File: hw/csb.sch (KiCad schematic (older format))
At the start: 31 parts

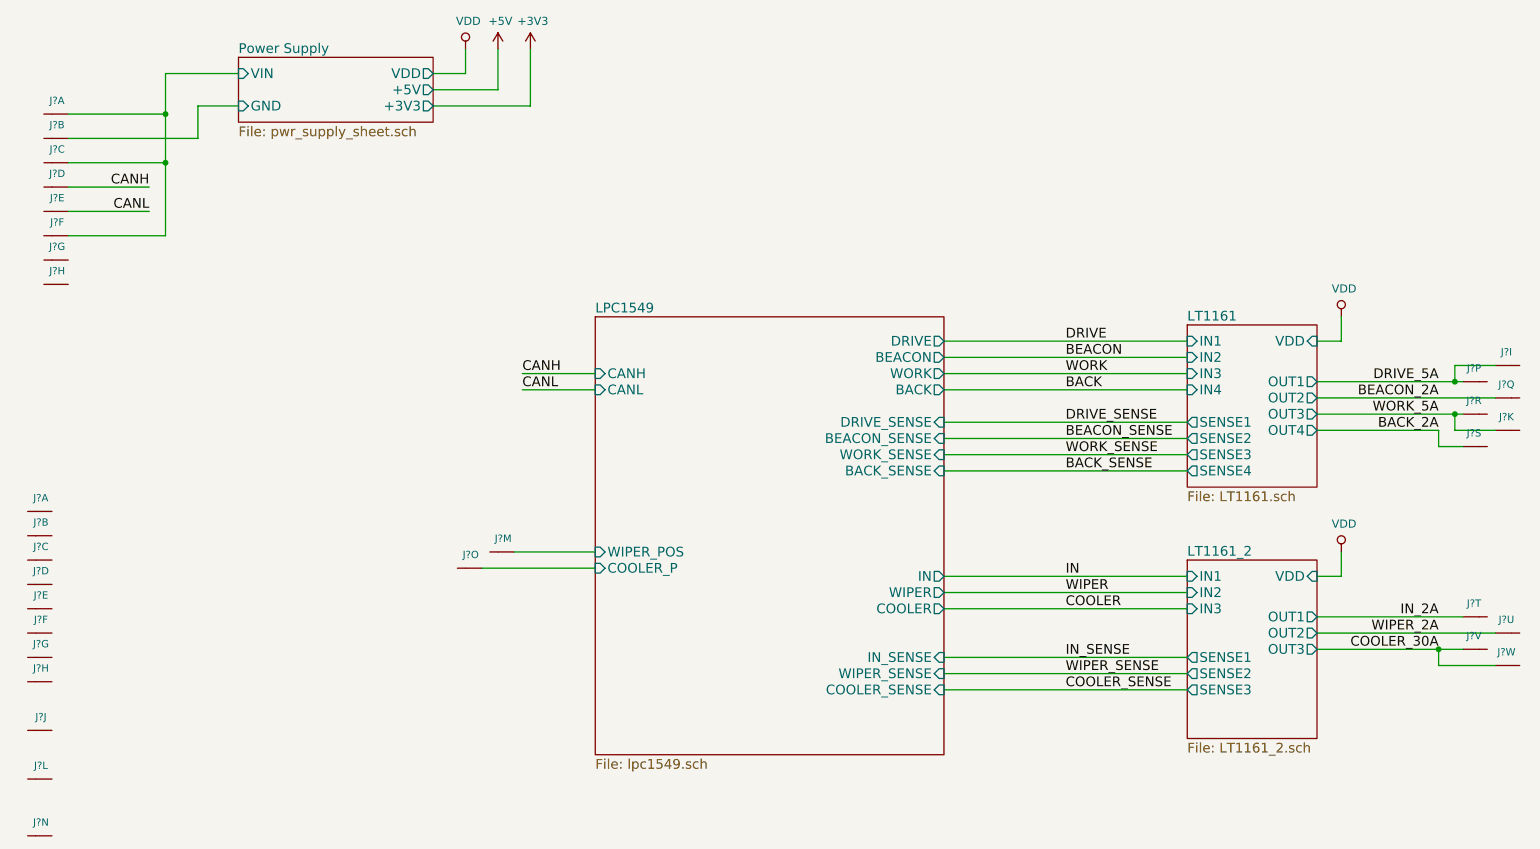
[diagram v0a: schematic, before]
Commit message: first pcb revision ready to order
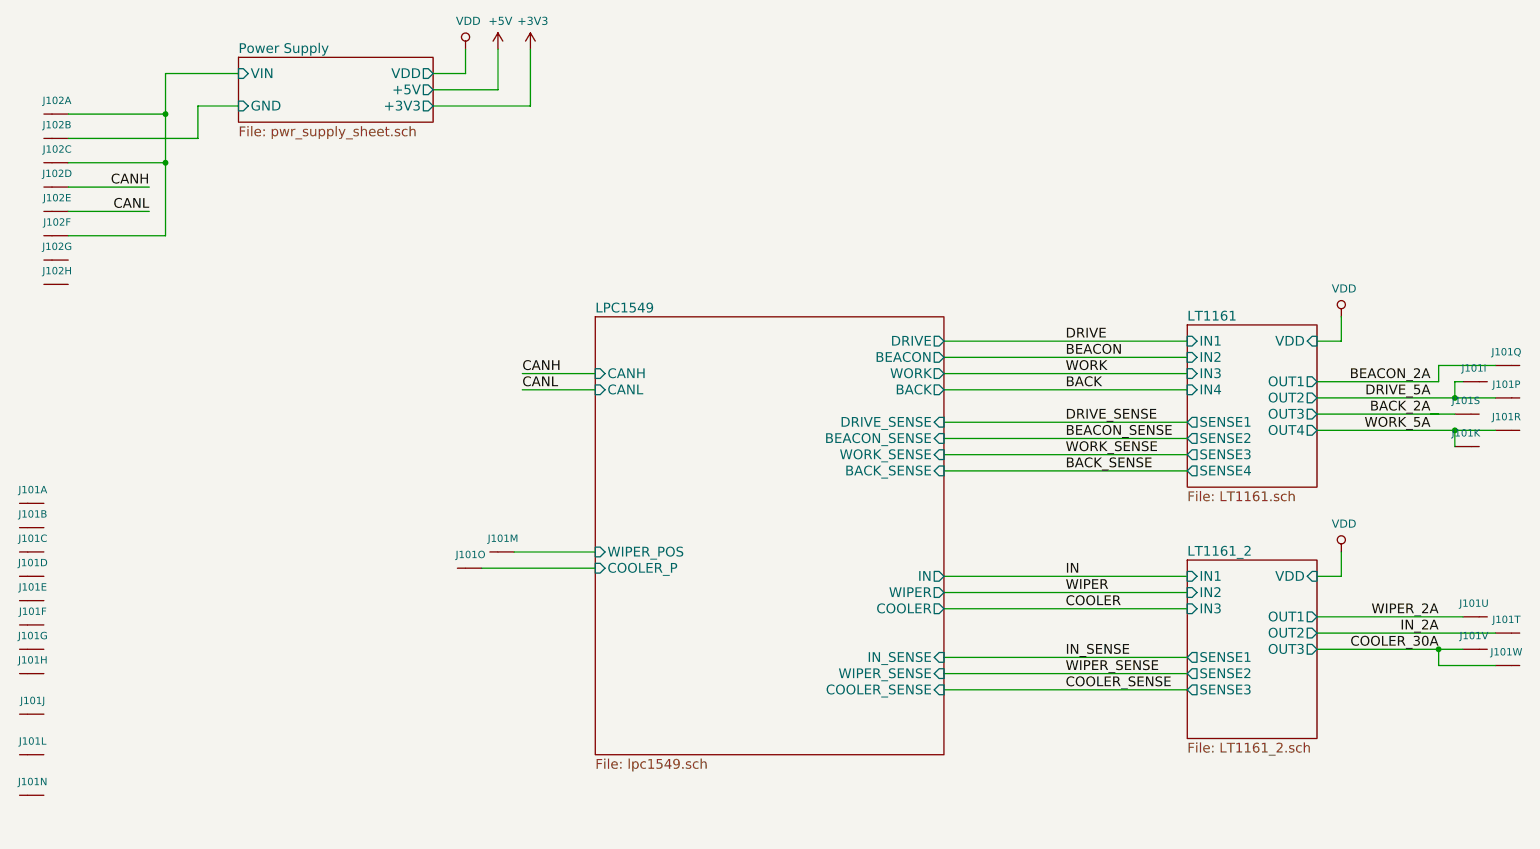
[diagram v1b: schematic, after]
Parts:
- removed J? (x23): AMPSEAL_23_POS_VERT_BLUE_SEALED_1-776228-5, usevolt:AMPSEAL_23_POS_H_1-776228-1, symbol AMPSEAL_23_POS_VERT_BLUE_SEALED_1-776228-5
- added J101: AMPSEAL_23_POS_VERT_BLUE_SEALED_1-776228-5, usevolt:AMPSEAL_23_POS_776200-1, symbol AMPSEAL_23_POS_VERT_BLUE_SEALED_1-776228-5
- gave numbers to parts that had none: 1
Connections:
- net BACK_2A: now also J101.P$19 (S)
- net BEACON_2A: now also J101.P$17 (S)
- net COOLER_30A: now also J101.P$22 (S), J101.P$23 (S)
- net DRIVE_5A: now also J101.P$16 (S), J101.P$9 (S)
- net IN_2A: now also J101.P$20 (S)
- net LPC1549/COOLER_P: now also J101.P$15 (S)
- net LPC1549/WIPER_POS: now also J101.P$13 (S)
- net WIPER_2A: now also J101.P$21 (S)
- net WORK_5A: now also J101.P$11 (S), J101.P$18 (S)

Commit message: sw directory created, oil cooler added in hw
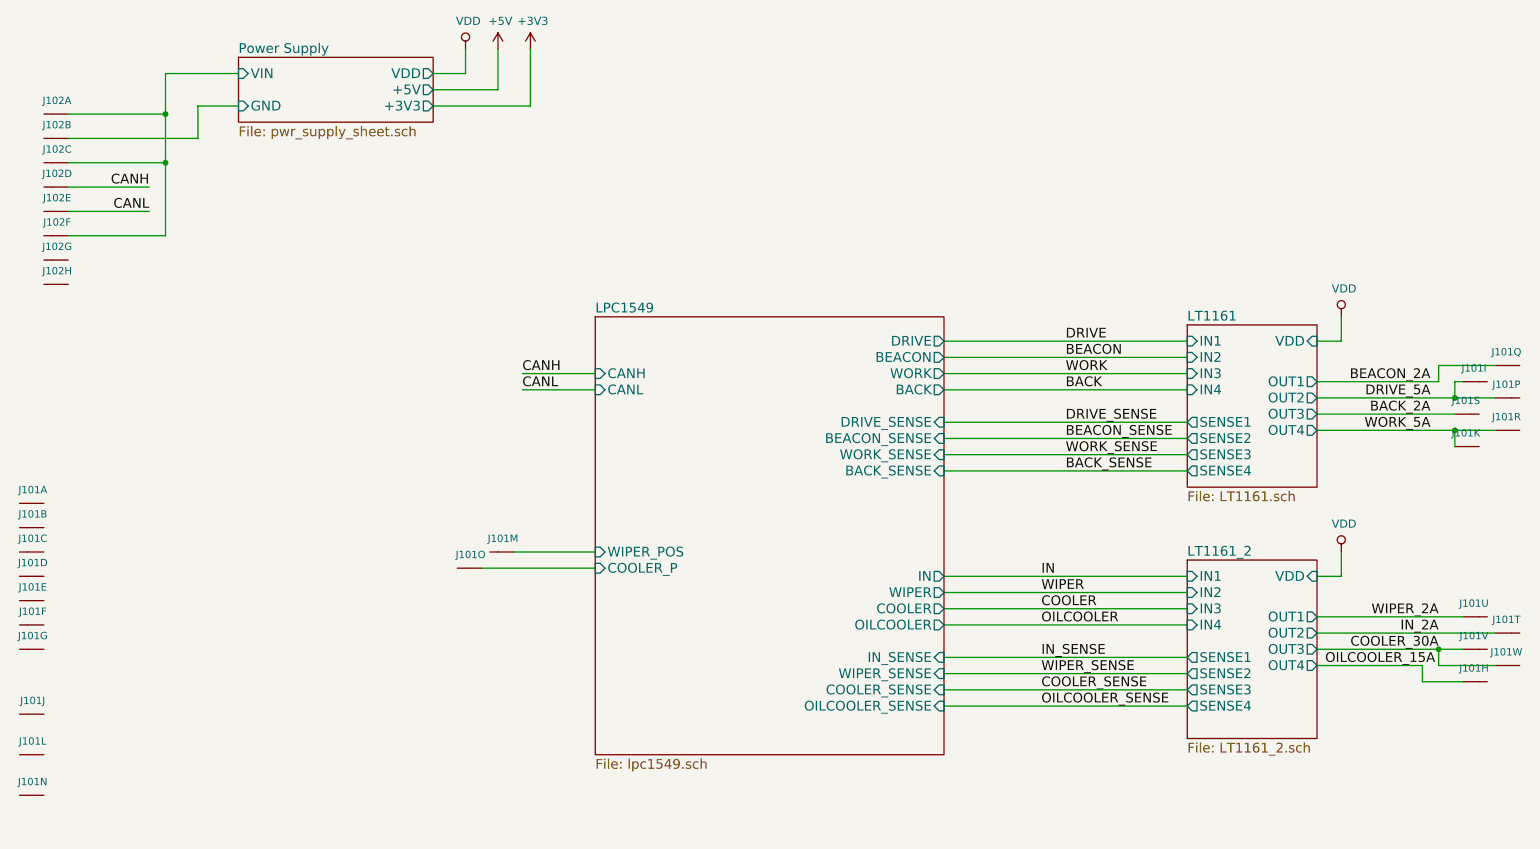
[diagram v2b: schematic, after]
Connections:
- net OILCOOLER_15A: now reaches J101.P$8 (S)
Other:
- moved on the sheet: J101H
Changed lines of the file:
@@
 $Descr A4 11693 8268
 encoding utf-8
-Sheet 1 12
+Sheet 1 13
 Title "Usewood Ceiling Supply Board"
 Date "2017-06-28"
@@
 Comment4 ""
 $EndDescr
-$Sheet
-S 4250 2800 2150 2700
-U 5953E91C
-F0 "LPC1549" 60
-F1 "lpc1549.sch" 60
-F2 "CANL" I L 4250 3250 60
-F3 "CANH" I L 4250 3150 60
-F4 "WIPER_POS" I L 4250 4250 60
-F5 "COOLER_P" I L 4250 4350 60
-F6 "DRIVE" O R 6400 2950 60
-F7 "WORK" O R 6400 3150 60
-F8 "IN" O R 6400 4400 60
-F9 "BACK" O R 6400 3250 60
-F10 "BEACON" O R 6400 3050 60
-F11 "WIPER" O R 6400 4500 60
-F12 "COOLER" O R 6400 4600 60
-F13 "WORK_SENSE" I R 6400 3650 60
-F14 "DRIVE_SENSE" I R 6400 3450 60
-F15 "IN_SENSE" I R 6400 4900 60
-F16 "BEACON_SENSE" I R 6400 3550 60
-F17 "BACK_SENSE" I R 6400 3750 60
-F18 "WIPER_SENSE" I R 6400 5000 60
-F19 "COOLER_SENSE" I R 6400 5100 60
-$EndSheet
 $Sheet
 S 2050 1200 1200 400
@@
 F10 "SENSE3" O L 7900 5100 60
 F11 "VDD" I R 8700 4400 60
+F12 "SENSE4" O L 7900 5200 60
+F13 "OUT4" O R 8700 4950 60
+F14 "IN4" I L 7900 4700 60
 $EndSheet
 $Comp
@@
 Text Label 9450 4850 2    60   ~ 0
 COOLER_30A
-Text Label 7150 4400 0    60   ~ 0
+Text Label 7000 4400 0    60   ~ 0
 IN
-Text Label 7150 4500 0    60   ~ 0
+Text Label 7000 4500 0    60   ~ 0
 WIPER
-Text Label 7150 4600 0    60   ~ 0
+Text Label 7000 4600 0    60   ~ 0
 COOLER
-Text Label 7150 4900 0    60   ~ 0
+Text Label 7000 4900 0    60   ~ 0
 IN_SENSE
-Text Label 7150 5000 0    60   ~ 0
+Text Label 7000 5000 0    60   ~ 0
 WIPER_SENSE
-Text Label 7150 5100 0    60   ~ 0
+Text Label 7000 5100 0    60   ~ 0
 COOLER_SENSE
 Text Label 7150 2950 0    60   ~ 0
@@
 Connection ~ 1600 1850
 Wire Wire Line
-	9400 3400 9550 3400
-Wire Wire Line
-	9450 3400 8700 3400
-Wire Wire Line
 	9550 3600 9550 3600
 Wire Wire Line
@@
 L AMPSEAL_23_POS_VERT_BLUE_SEALED_1-776228-5 J101
 U 8 1 595D3EB6
-P 750 5000
-F 0 "J101" H 718 5083 45  0000 C CNN
-F 1 "AMPSEAL_23_POS_VERT_BLUE_SEALED_1-776228-5" H 750 5000 45  0001 L BNN
-F 2 "usevolt:AMPSEAL_23_POS_776200-1" H 780 5150 20  0001 C CNN
-F 3 "http://www.mouser.com/ds/2/418/NG_CD_776228_C13-683129.pdf" H 850 4970 60  0001 C CNN
-F 4 "571-1-776228-5" H 1250 5370 60  0001 C CNN "1st Source Part Number"
-F 5 "1-776228-5" H 1050 5170 60  0001 C CNN "Manufacturer Part Number"
-F 6 "Mouser" H 1150 5270 60  0001 C CNN "1st Source"
-F 7 "TE Connectivity" H 950 5070 60  0001 C CNN "Manufacturer"
-	8    750  5000
-	-1   0    0    -1
+P 9700 5050
+F 0 "J101" H 9668 5133 45  0000 C CNN
+F 1 "AMPSEAL_23_POS_VERT_BLUE_SEALED_1-776228-5" H 9700 5050 45  0001 L BNN
+F 2 "usevolt:AMPSEAL_23_POS_776200-1" H 9730 5200 20  0001 C CNN
+F 3 "http://www.mouser.com/ds/2/418/NG_CD_776228_C13-683129.pdf" H 9800 5020 60  0001 C CNN
+F 4 "571-1-776228-5" H 10200 5420 60  0001 C CNN "1st Source Part Number"
+F 5 "1-776228-5" H 10000 5220 60  0001 C CNN "Manufacturer Part Number"
+F 6 "Mouser" H 10100 5320 60  0001 C CNN "1st Source"
+F 7 "TE Connectivity" H 9900 5120 60  0001 C CNN "Manufacturer"
+	8    9700 5050
+	1    0    0    -1
 $EndComp
 $Comp
@@
 Wire Wire Line
 	9450 3100 9800 3100
+Wire Wire Line
+	9550 3400 8700 3400
+$Sheet
+S 4250 2800 2150 2700
+U 5953E91C
+F0 "LPC1549" 60
+F1 "lpc1549.sch" 60
+F2 "CANL" I L 4250 3250 60
+F3 "CANH" I L 4250 3150 60
+F4 "WIPER_POS" I L 4250 4250 60
+F5 "COOLER_P" I L 4250 4350 60
+F6 "DRIVE" O R 6400 2950 60
+F7 "WORK" O R 6400 3150 60
+F8 "IN" O R 6400 4400 60
+F9 "BACK" O R 6400 3250 60
+F10 "BEACON" O R 6400 3050 60
+F11 "WIPER" O R 6400 4500 60
+F12 "COOLER" O R 6400 4600 60
+F13 "WORK_SENSE" I R 6400 3650 60
+F14 "DRIVE_SENSE" I R 6400 3450 60
+F15 "IN_SENSE" I R 6400 4900 60
+F16 "BEACON_SENSE" I R 6400 3550 60
+F17 "BACK_SENSE" I R 6400 3750 60
+F18 "WIPER_SENSE" I R 6400 5000 60
+F19 "COOLER_SENSE" I R 6400 5100 60
+F20 "OILCOOLER_SENSE" I R 6400 5200 60
+F21 "OILCOOLER" O R 6400 4700 60
+$EndSheet
+Wire Wire Line
+	6400 4700 7900 4700
+Wire Wire Line
+	7900 5200 6400 5200
+Text Label 7000 4700 0    60   ~ 0
+OILCOOLER
+Text Label 7000 5200 0    60   ~ 0
+OILCOOLER_SENSE
+Wire Wire Line
+	9600 5050 9350 5050
+Wire Wire Line
+	9350 5050 9350 4950
+Wire Wire Line
+	9350 4950 8700 4950
+Text Label 8750 4950 0    60   ~ 0
+OILCOOLER_15A
 $EndSCHEMATC
